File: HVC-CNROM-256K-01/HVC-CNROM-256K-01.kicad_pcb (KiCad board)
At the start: 2 copper layers, 90.5 x 56.8 mm, 1 part

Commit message: Add extra outlines; Update modules to KiCad 6
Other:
- net class Default removed

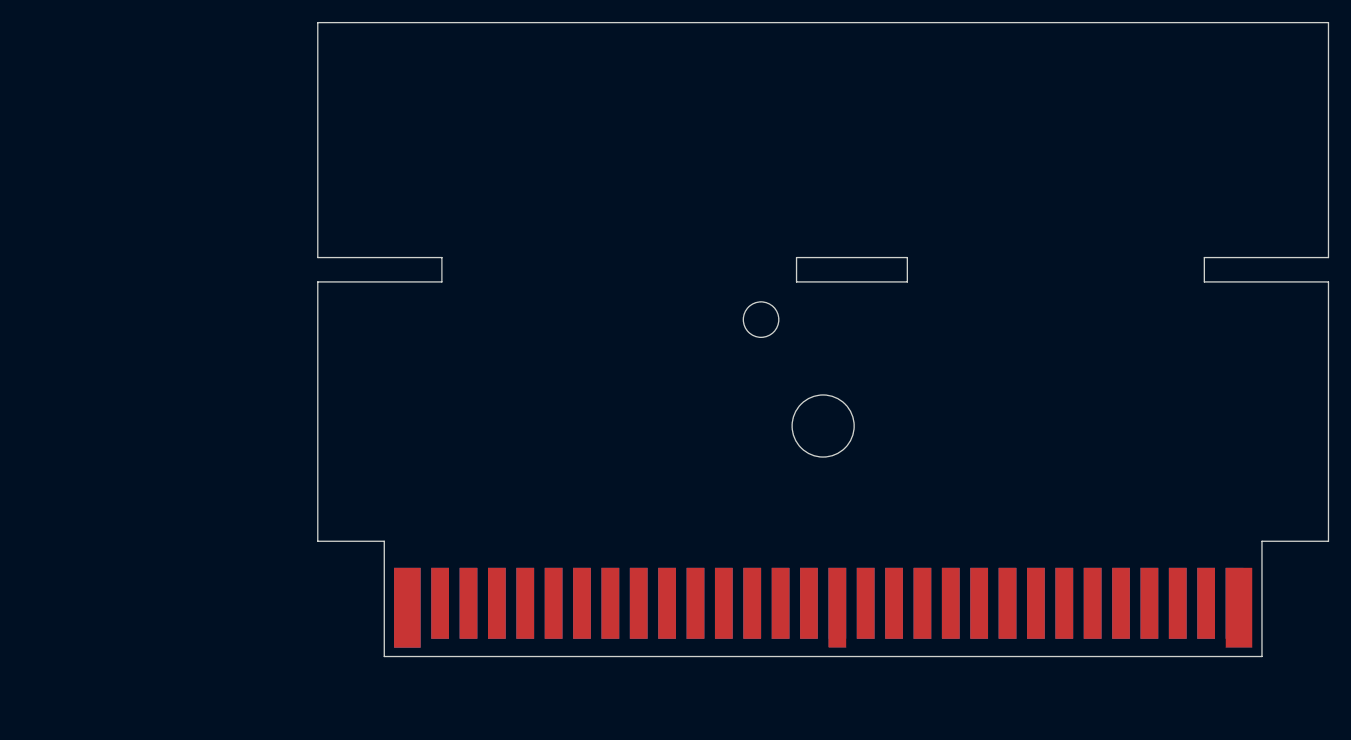
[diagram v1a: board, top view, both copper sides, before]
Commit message: Update HVC-CxROM measurements
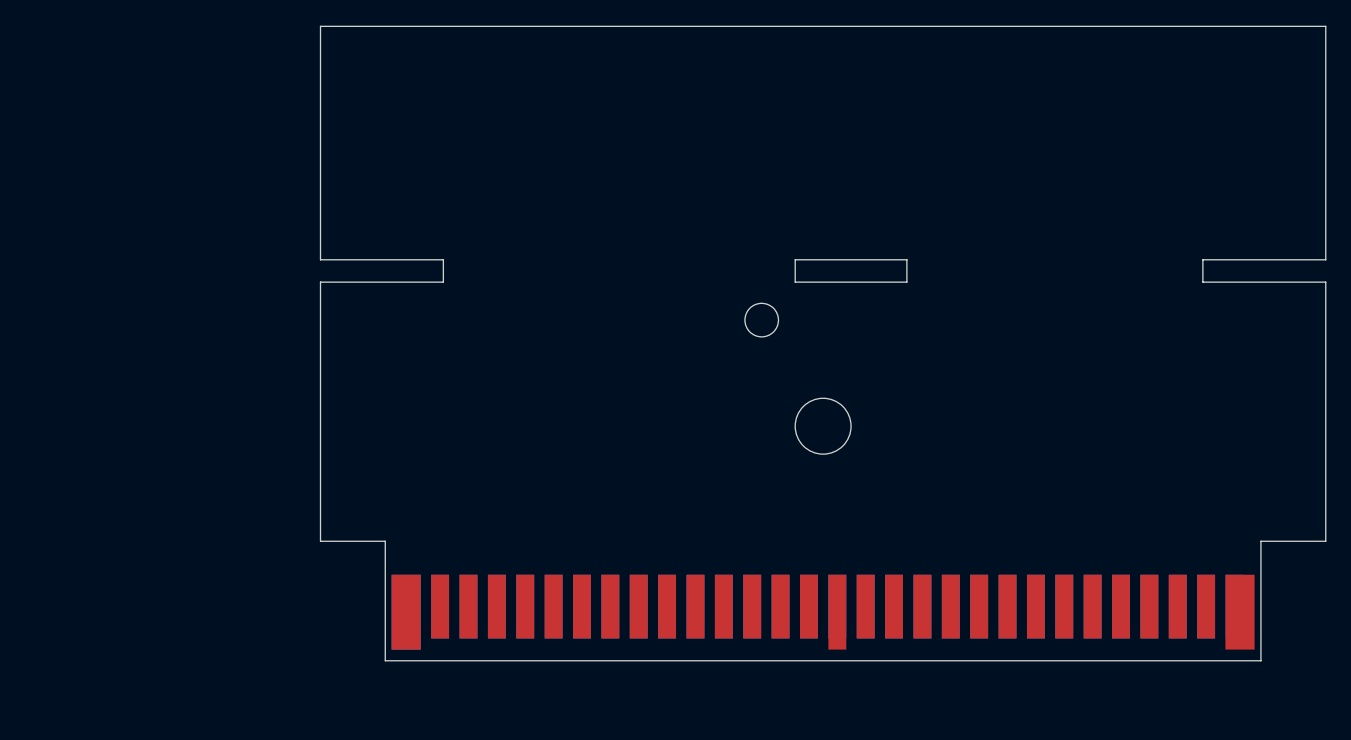
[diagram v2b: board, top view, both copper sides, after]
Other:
- board size 90.5 x 56.8 mm -> 90 x 56.8 mm

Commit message: Update origin to 127, 127 mm
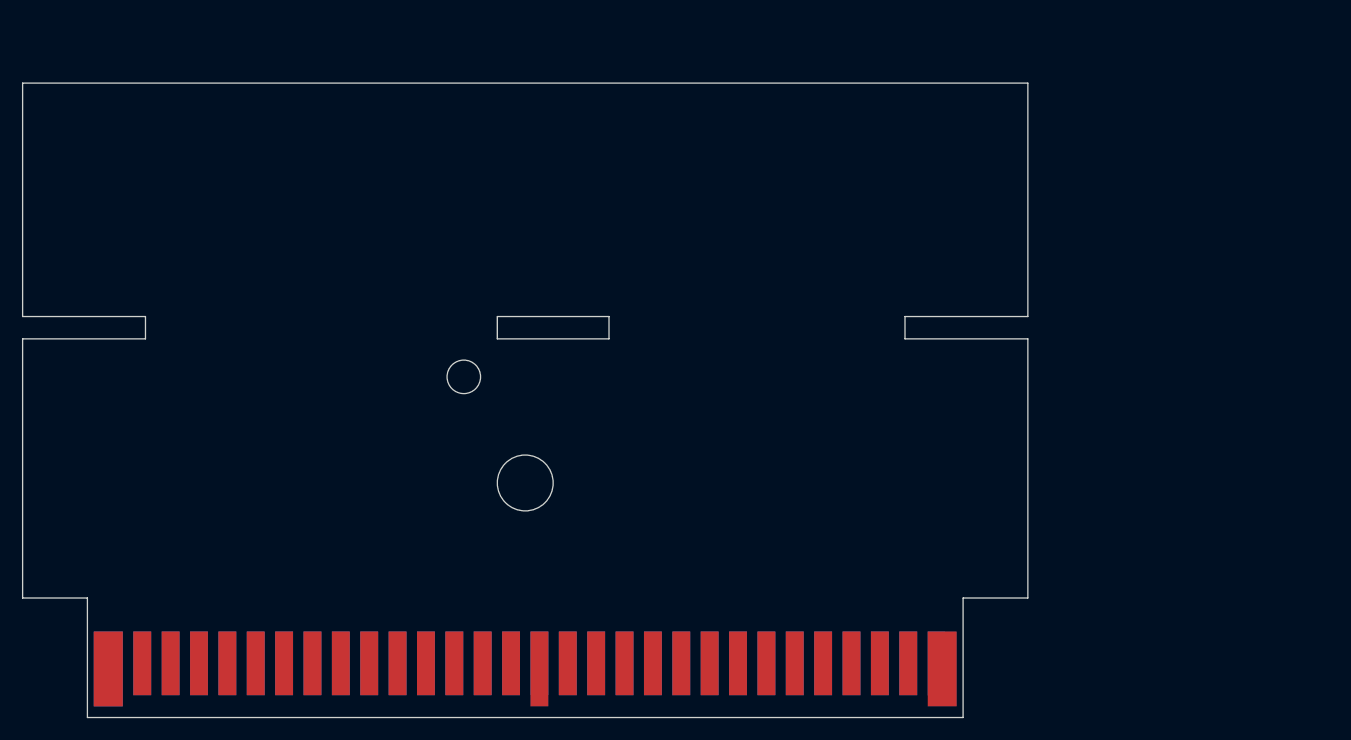
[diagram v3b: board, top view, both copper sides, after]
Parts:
- moved REF** 27.1 mm to (127.0, 127.0)
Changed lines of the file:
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@@
   )
   (layers
-    (0 "F.Cu" signal)
+    (0 "F.Cu" mixed)
     (31 "B.Cu" signal)
     (32 "B.Adhes" user "B.Adhesive")
@@
     )
     (pad_to_mask_clearance 0)
-    (grid_origin 153.67 121.92)
+    (grid_origin 127 127)
     (pcbplotparams
       (layerselection 0x00010fc_ffffffff)
@@
   (net 0 "")
   (footprint "card-edge-connectors:HVC-CNROM-256K-01" locked (layer "F.Cu")
-    (at 153.67 121.92)
+    (at 127 127)
     (attr through_hole)
-    (fp_text reference "REF**" (at 0 0) (layer "F.Fab")
+    (fp_text reference "REF**" (at -26.67 5.26) (layer "F.Fab")
       (effects (font (size 1 1) (thickness 0.15)))
     )
-    (fp_text value "HVC-CNROM-256K-01" (at 0 11.43) (layer "F.Fab")
+    (fp_text value "HVC-CNROM-256K-01" (at -26.67 16.69) (layer "F.Fab")
       (effects (font (size 1 1) (thickness 0.15)))
     )
@@
     (pad "60" connect rect locked (at 36.83 5.85) (size 1.6 5.7) (layers "B.Cu"))
   )
-  (gr_line (start 151.17 98.72) (end 151.17 96.72) (layer "Edge.Cuts") (width 0.05))
-  (gr_line (start 119.67 98.72) (end 119.67 96.72) (layer "Edge.Cuts") (width 0.05))
-  (gr_line (start 187.67 98.72) (end 187.67 96.72) (layer "Edge.Cuts") (width 0.05))
-  (gr_line (start 108.67 96.720001) (end 119.67 96.72) (layer "Edge.Cuts") (width 0.05))
-  (gr_line (start 108.67 98.72) (end 108.67 121.92) (layer "Edge.Cuts") (width 0.05))
-  (gr_line (start 198.67 96.72) (end 187.67 96.72) (layer "Edge.Cuts") (width 0.05))
-  (gr_line (start 161.17 96.72) (end 151.17 96.72) (layer "Edge.Cuts") (width 0.05))
-  (gr_line (start 151.17 98.72) (end 161.17 98.72) (layer "Edge.Cuts") (width 0.05))
-  (gr_line (start 161.17 96.72) (end 161.17 98.72) (layer "Edge.Cuts") (width 0.05))
-  (gr_line (start 198.67 98.72) (end 187.67 98.72) (layer "Edge.Cuts") (width 0.05))
-  (gr_line (start 198.67 96.72) (end 198.67 75.82) (layer "Edge.Cuts") (width 0.05))
-  (gr_line (start 108.67 75.82) (end 108.67 96.720001) (layer "Edge.Cuts") (width 0.05))
-  (gr_circle (center 153.67 111.62) (end 156.17 111.62) (layer "Edge.Cuts") (width 0.05) (fill none))
-  (gr_line (start 192.87 121.92) (end 198.67 121.92) (layer "Edge.Cuts") (width 0.05))
-  (gr_line (start 114.47 132.62) (end 192.87 132.62) (layer "Edge.Cuts") (width 0.05))
-  (gr_circle (center 148.17 102.12) (end 149.67 102.12) (layer "Edge.Cuts") (width 0.05) (fill none))
-  (gr_line (start 192.87 132.62) (end 192.87 121.92) (layer "Edge.Cuts") (width 0.05))
-  (gr_line (start 108.67 121.92) (end 114.47 121.92) (layer "Edge.Cuts") (width 0.05))
-  (gr_line (start 198.67 121.92) (end 198.67 98.72) (layer "Edge.Cuts") (width 0.05))
-  (gr_line (start 114.47 121.92) (end 114.47 132.62) (layer "Edge.Cuts") (width 0.05))
-  (gr_line (start 119.67 98.72) (end 108.67 98.72) (layer "Edge.Cuts") (width 0.05))
-  (gr_line (start 198.67 75.82) (end 108.67 75.82) (layer "Edge.Cuts") (width 0.05))
+  (gr_line (start 87.8 127) (end 87.8 137.7) (layer "Edge.Cuts") (width 0.05))
+  (gr_line (start 93 103.8) (end 82 103.8) (layer "Edge.Cuts") (width 0.05))
+  (gr_line (start 93 101.8) (end 93 103.8) (layer "Edge.Cuts") (width 0.05))
+  (gr_line (start 172 101.8) (end 172 80.9) (layer "Edge.Cuts") (width 0.05))
+  (gr_line (start 172 80.9) (end 82 80.9) (layer "Edge.Cuts") (width 0.05))
+  (gr_line (start 87.8 137.7) (end 166.2 137.7) (layer "Edge.Cuts") (width 0.05))
+  (gr_line (start 161 103.8) (end 161 101.8) (layer "Edge.Cuts") (width 0.05))
+  (gr_line (start 82 101.8) (end 93 101.8) (layer "Edge.Cuts") (width 0.05))
+  (gr_line (start 161 101.8) (end 172 101.8) (layer "Edge.Cuts") (width 0.05))
+  (gr_line (start 166.2 137.7) (end 166.2 127) (layer "Edge.Cuts") (width 0.05))
+  (gr_line (start 124.5 103.8) (end 134.5 103.8) (layer "Edge.Cuts") (width 0.05))
+  (gr_line (start 82 103.8) (end 82 127) (layer "Edge.Cuts") (width 0.05))
+  (gr_line (start 82 127) (end 87.8 127) (layer "Edge.Cuts") (width 0.05))
+  (gr_line (start 134.5 103.8) (end 134.5 101.8) (layer "Edge.Cuts") (width 0.05))
+  (gr_line (start 172 127) (end 172 103.8) (layer "Edge.Cuts") (width 0.05))
+  (gr_circle (center 121.5 107.2) (end 123 107.2) (layer "Edge.Cuts") (width 0.05) (fill none))
+  (gr_line (start 134.5 101.8) (end 124.5 101.8) (layer "Edge.Cuts") (width 0.05))
+  (gr_line (start 82 80.9) (end 82 101.8) (layer "Edge.Cuts") (width 0.05))
+  (gr_line (start 124.5 101.8) (end 124.5 103.8) (layer "Edge.Cuts") (width 0.05))
+  (gr_line (start 172 103.8) (end 161 103.8) (layer "Edge.Cuts") (width 0.05))
+  (gr_circle (center 127 116.7) (end 129.5 116.7) (layer "Edge.Cuts") (width 0.05) (fill none))
+  (gr_line (start 166.2 127) (end 172 127) (layer "Edge.Cuts") (width 0.05))
 )
